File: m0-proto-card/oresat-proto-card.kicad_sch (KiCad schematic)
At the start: 0 parts

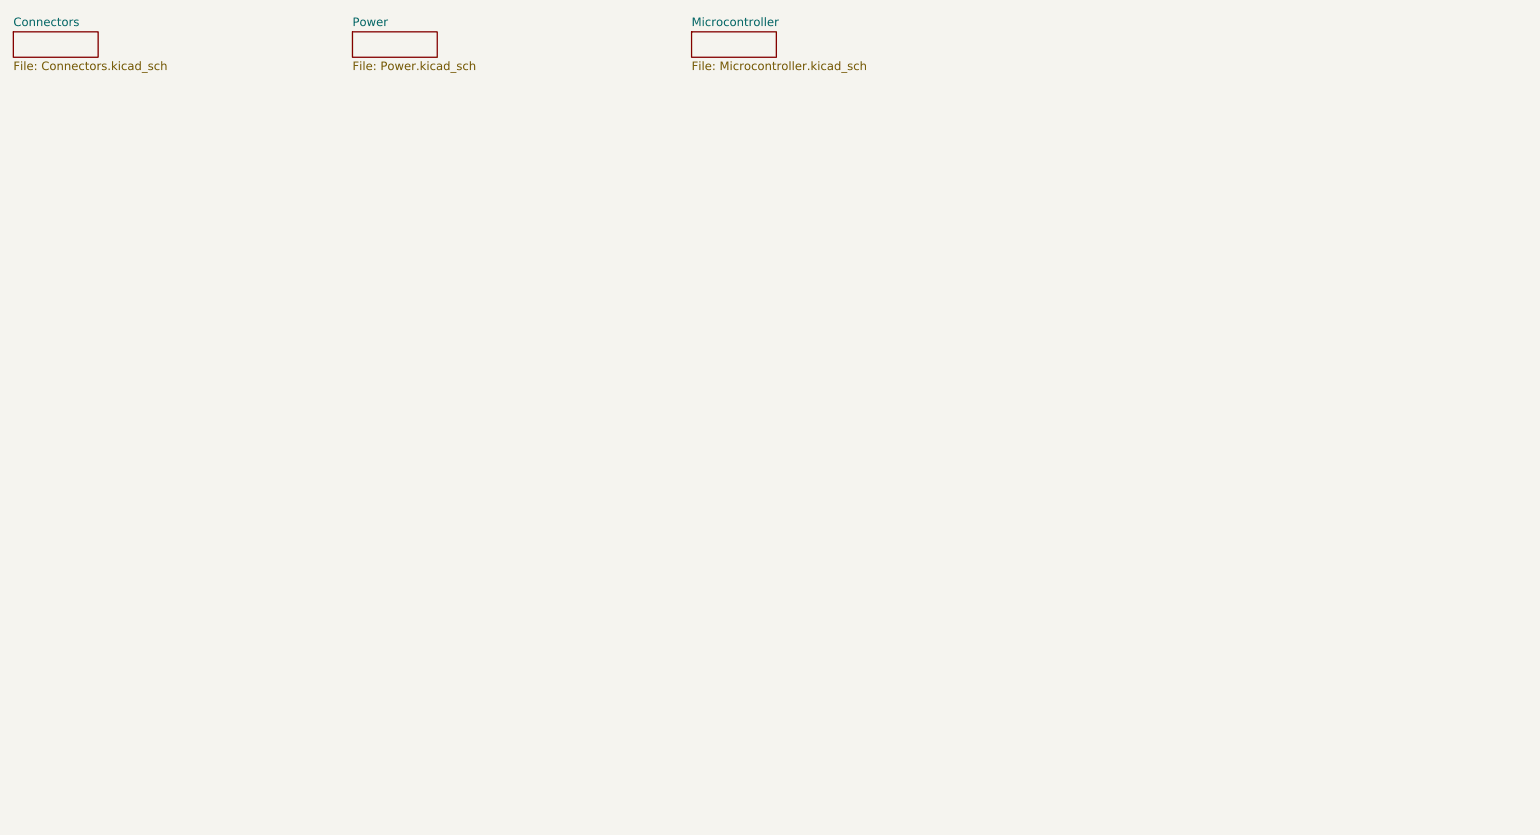
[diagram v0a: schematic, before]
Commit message: More cleanup, and renaming of files, and better page layout
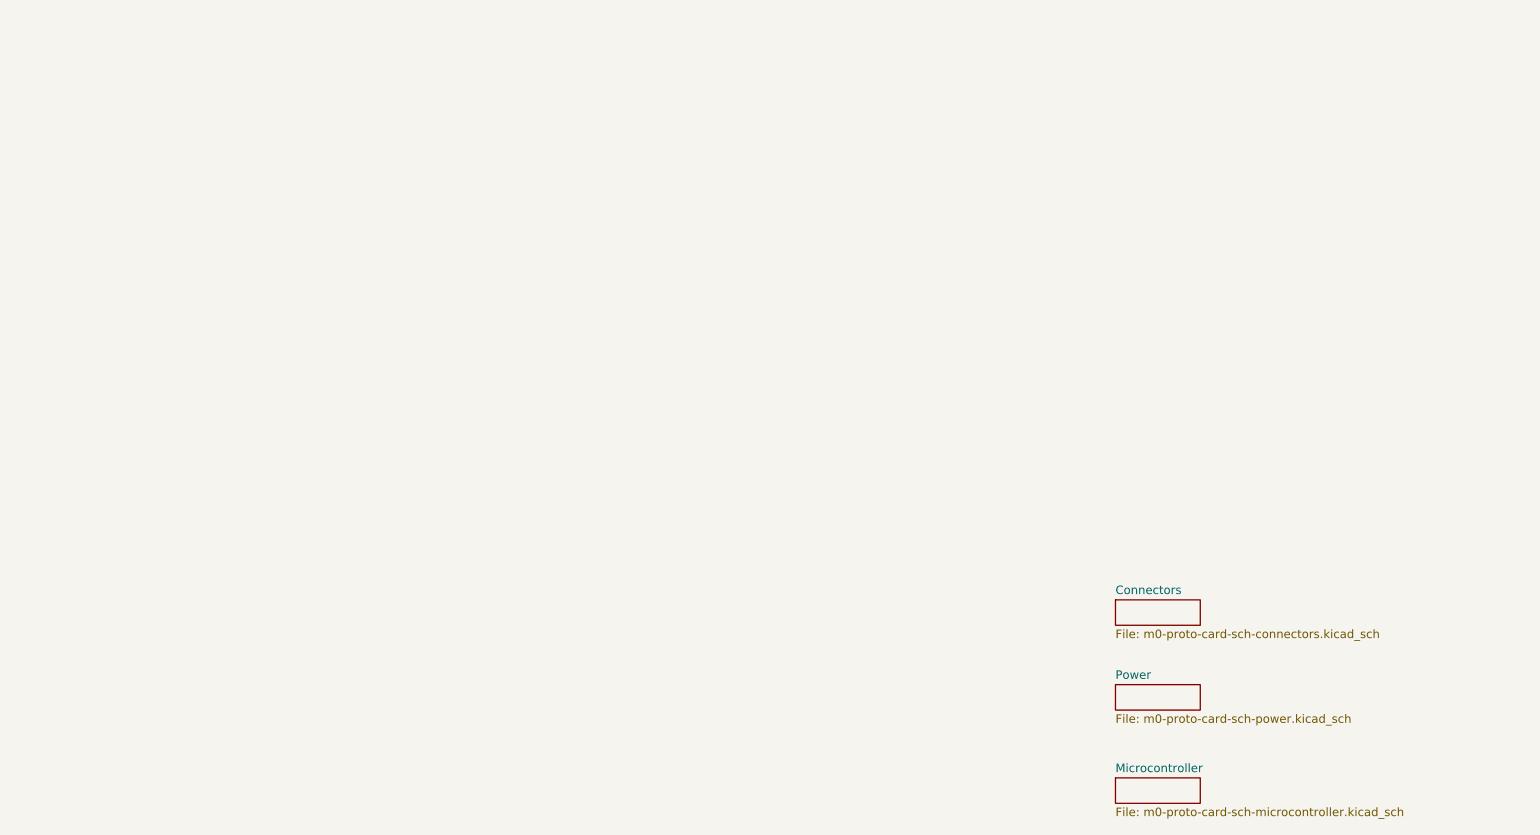
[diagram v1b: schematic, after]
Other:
- sheet Connectors: file Connectors.kicad_sch -> m0-proto-card-sch-connectors.kicad_sch
- sheet Microcontroller: file Microcontroller.kicad_sch -> m0-proto-card-sch-microcontroller.kicad_sch
- sheet Power: file Power.kicad_sch -> m0-proto-card-sch-power.kicad_sch
- title: oresat-proto-card -> OreSat M0 Proto Card
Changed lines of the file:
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@@
 (kicad_sch (version 20230121) (generator eeschema)
-  (paper "User" 469.9 317.627)
+  (paper "USLedger")
   (title_block
-    (title "oresat-proto-card")
-    (date "2024-02-25")
+    (title "OreSat M0 Proto Card")
+    (date "2024-03-21")
     (rev "5.0")
   )
-  (sheet (at 25.4 25.4) (size 12.7 3.81) (fields_autoplaced)
+  (sheet (at 190.5 110.49) (size 12.7 3.81) (fields_autoplaced)
     (stroke (width 0) (type solid))
     (fill (color 0 0 0 0.0000))
-    (property "Sheetname" "Connectors" (at 25.4 24.6884 0)
+    (property "Sheetname" "Connectors" (at 190.5 109.7784 0)
       (effects (font (size 1.27 1.27)) (justify left bottom))
     )
-    (property "Sheetfile" "Connectors.kicad_sch" (at 25.4 29.7946 0)
+    (property "Sheetfile" "m0-proto-card-sch-connectors.kicad_sch" (at 190.5 114.8846 0)
       (effects (font (size 1.27 1.27)) (justify left top))
     )
@@
     )
   )
-  (sheet (at 76.2 25.4) (size 12.7 3.81) (fields_autoplaced)
+  (sheet (at 190.5 123.19) (size 12.7 3.81) (fields_autoplaced)
     (stroke (width 0) (type solid))
     (fill (color 0 0 0 0.0000))
-    (property "Sheetname" "Power" (at 76.2 24.6884 0)
+    (property "Sheetname" "Power" (at 190.5 122.4784 0)
       (effects (font (size 1.27 1.27)) (justify left bottom))
     )
-    (property "Sheetfile" "Power.kicad_sch" (at 76.2 29.7946 0)
+    (property "Sheetfile" "m0-proto-card-sch-power.kicad_sch" (at 190.5 127.5846 0)
       (effects (font (size 1.27 1.27)) (justify left top))
     )
@@
     )
   )
-  (sheet (at 127 25.4) (size 12.7 3.81) (fields_autoplaced)
+  (sheet (at 190.5 137.16) (size 12.7 3.81) (fields_autoplaced)
     (stroke (width 0) (type solid))
     (fill (color 0 0 0 0.0000))
-    (property "Sheetname" "Microcontroller" (at 127 24.6884 0)
+    (property "Sheetname" "Microcontroller" (at 190.5 136.4484 0)
       (effects (font (size 1.27 1.27)) (justify left bottom))
     )
-    (property "Sheetfile" "Microcontroller.kicad_sch" (at 127 29.7946 0)
+    (property "Sheetfile" "m0-proto-card-sch-microcontroller.kicad_sch" (at 190.5 141.5546 0)
       (effects (font (size 1.27 1.27)) (justify left top))
     )
